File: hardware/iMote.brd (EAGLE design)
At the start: 43 x 50 mm, 50 parts, among them CN1 USB-MINIB-UX60SC-MB, CN2 ICSP, CN3 CC-HEADER, IC1 ATmega328P-AU, IC2 BLE112-A-VISUAL, IC3 FT232RLSSOP, Q1 16MHz, T1 2SC1815

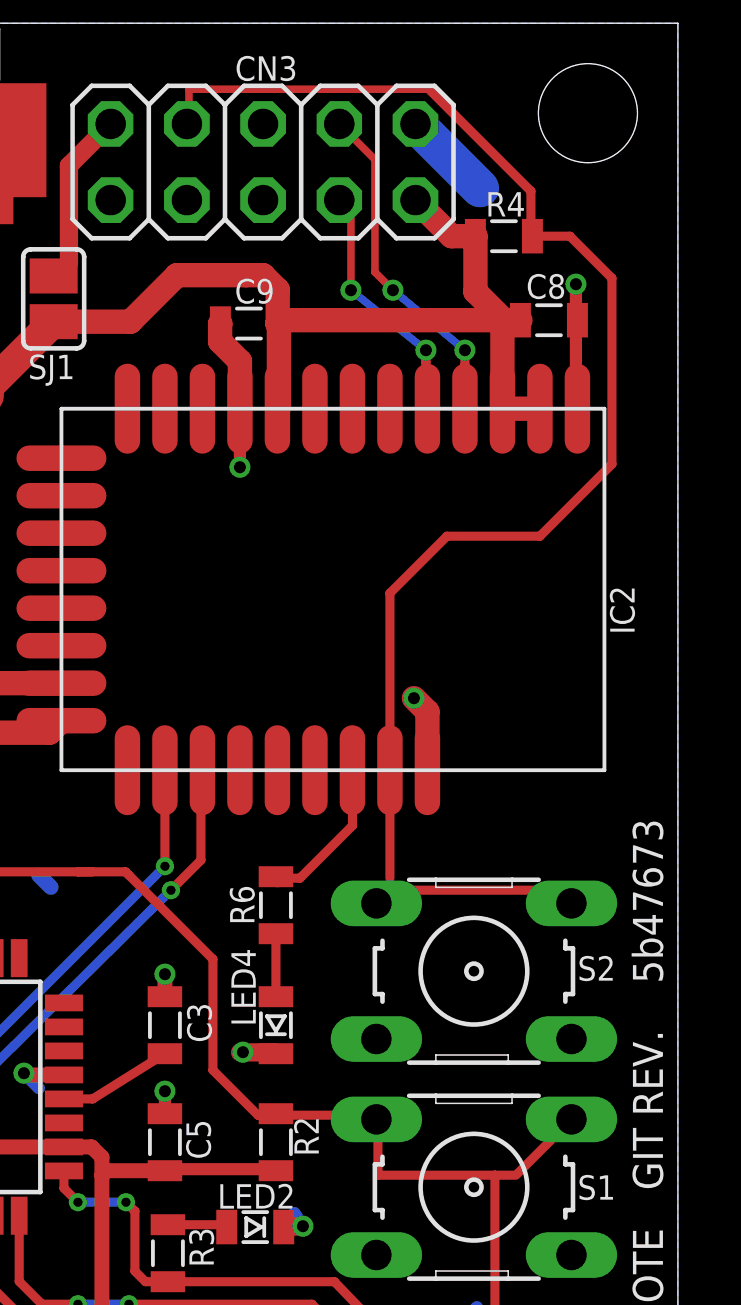
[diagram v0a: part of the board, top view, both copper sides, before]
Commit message: ble112をリセットするためのS2スイッチをなくして、 AVRの!RESET(5V)を分圧して3V程度にしてからble112の!BLE/RSTにつなぐ これはFT232RLのDTRからつながってるからUSB通したシリアル通信をしようとするときに AVRのリセットと同時にble112もリセットするから AVRの起動後からble112とのシリアル通信がうまくいく (この変更を行うまでは,シリアル通信開始時に必ずS2スイッチを押す必要があった)
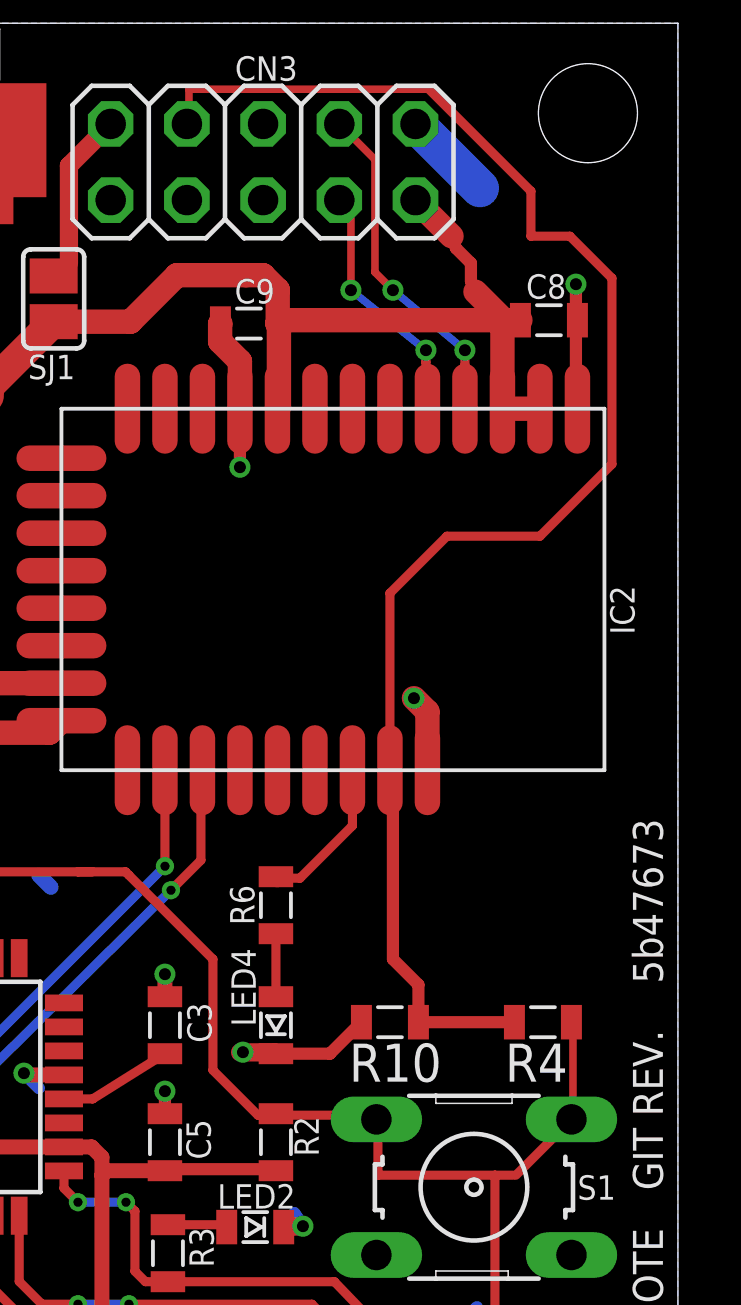
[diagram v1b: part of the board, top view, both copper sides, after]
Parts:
- removed S2: B3F-1000, switch-omron:B3F-10XX
- added R10: 22k, my:2012
- R4: value 1K -> 10k
- moved R4 26.2 mm to (38.5, 16.7)
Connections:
- net !BLE/RST: now also R10.2, R4.2; no longer R4.1, S2.1, S2.2
- net !RESET: now also R4.1
- net +3V3: no longer R4.2
- net GND: now also R10.1; no longer S2.3, S2.4
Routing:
- net !RESET: track 43.4 -> 46.8 mm
- net GND: track 90.2 -> 93.5 mm
- net +3V3: track 60.6 -> 60.1 mm
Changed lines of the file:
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@@
 <attribute name="VALUE" x="29.462" y="42.274" size="1.27" layer="27" rot="R180"/>
-</element>
-<element name="R4" library="my" package="2012" value="1K" x="37.2" y="42.9" smashed="yes" rot="R180">
-<attribute name="NAME" x="36.586" y="43.556" size="0.8128" layer="25"/>
-<attribute name="VALUE" x="37.962" y="45.186" size="1.27" layer="27" rot="R180"/>
-</element>
-<element name="S2" library="switch-omron" package="B3F-10XX" value="B3F-1000" x="36.2" y="18.4" smashed="yes">
-<attribute name="OC_NEWARK" value="36M3542" x="16.2" y="28.4" size="1.778" layer="27" display="off"/>
-<attribute name="MPN" value="B3F-1000" x="16.2" y="28.4" size="1.778" layer="27" display="off"/>
-<attribute name="MF" value="" x="16.2" y="28.4" size="1.778" layer="27" display="off"/>
-<attribute name="OC_FARNELL" value="176432" x="16.2" y="28.4" size="1.778" layer="27" display="off"/>
-<attribute name="NAME" x="39.652" y="18.083" size="0.8128" layer="25" ratio="10"/>
-<attribute name="VALUE" x="33.152" y="13.32" size="1.27" layer="27" ratio="10"/>
 </element>
 <element name="R5" library="my" package="2012" value="330" x="16" y="28" smashed="yes" rot="R270">
@@
 <attribute name="NAME" x="24.0038" y="0.0588" size="0.8128" layer="25" ratio="10"/>
 <attribute name="VALUE" x="22.58" y="-0.845" size="1.27" layer="27"/>
+</element>
+<element name="R4" library="my" package="2012" value="10k" x="38.5" y="16.7" smashed="yes" rot="R180">
+<attribute name="NAME" x="37.238" y="14.716" size="1.27" layer="25"/>
+<attribute name="VALUE" x="39.262" y="18.986" size="1.27" layer="27" rot="R180"/>
+</element>
+<element name="R10" library="my" package="2012" value="22k" x="33.4" y="16.7" smashed="yes">
+<attribute name="NAME" x="32.038" y="14.716" size="1.27" layer="25"/>
+<attribute name="VALUE" x="32.638" y="14.414" size="1.27" layer="27"/>
 </element>
 </elements>
@@
 <contactref element="C13" pad="2"/>
 <contactref element="S1" pad="1"/>
-<contactref element="S1" pad="2"/>
 <wire x1="39.4" y1="13.4" x2="37.6" y2="11.6" width="0.3048" layer="1"/>
 <wire x1="35.6" y1="2.4" x2="35.54" y2="2.33" width="0.254" layer="1"/>
-<wire x1="39.4" y1="13.4" x2="39.4512" y2="13.4606" width="0.254" layer="1"/>
 <wire x1="33" y1="11.6" x2="36.9" y2="11.6" width="0.3048" layer="1"/>
 <wire x1="36.9" y1="11.6" x2="37.5" y2="11.6" width="0.3048" layer="1"/>
@@
 <wire x1="35.6" y1="2.4" x2="36.9" y2="3.7" width="0.3048" layer="1"/>
 <wire x1="36.9" y1="3.7" x2="36.9" y2="11.6" width="0.3048" layer="1"/>
+<contactref element="S1" pad="2"/>
+<contactref element="R4" pad="1"/>
+<wire x1="39.5" y1="13.5" x2="39.4512" y2="13.4606" width="0.254" layer="1"/>
+<wire x1="39.5" y1="13.5" x2="39.4" y2="13.4" width="0.254" layer="1"/>
+<wire x1="39.5" y1="13.6" x2="39.5" y2="16.7" width="0.254" layer="1"/>
+<wire x1="39.5" y1="16.7" x2="39.45" y2="16.7" width="0.254" layer="1"/>
+<wire x1="39.5" y1="13.6" x2="39.4512" y2="13.4606" width="0.254" layer="1"/>
 </signal>
 <signal name="D11/MOSI">
@@
 <contactref element="C10" pad="2"/>
 <contactref element="C9" pad="2"/>
-<contactref element="S2" pad="3"/>
 <contactref element="LED3" pad="C"/>
 <contactref element="LED4" pad="C"/>
@@
 <contactref element="IC3" pad="18"/>
 <contactref element="S1" pad="4"/>
-<contactref element="S2" pad="4"/>
 <contactref element="IC1" pad="21"/>
 <contactref element="C5" pad="1"/>
@@
 <wire x1="22.05" y1="26.35" x2="19" y2="26.35" width="0.8128" layer="1"/>
 <wire x1="30.5" y1="9.9" x2="30.21575" y2="10.33793125" width="0.4064" layer="16"/>
+<contactref element="R10" pad="1"/>
+<wire x1="29.6" y1="15.65" x2="31.4" y2="15.65" width="0.4064" layer="1"/>
+<wire x1="31.4" y1="15.65" x2="32.45" y2="16.7" width="0.4064" layer="1"/>
 </signal>
 <signal name="N$10">
@@
 <contactref element="IC2" pad="DVDD"/>
 <contactref element="C10" pad="1"/>
-<contactref element="R4" pad="2"/>
 <contactref element="R5" pad="1"/>
 <contactref element="CN3" pad="2"/>
@@
 <wire x1="29.8" y1="40.1" x2="37.2" y2="40.1" width="0.8128" layer="1"/>
 <wire x1="37.2" y1="40.1" x2="37.75" y2="40.1" width="0.8128" layer="1"/>
-<wire x1="36.25" y1="42.9" x2="36.25" y2="41.05" width="0.8128" layer="1"/>
 <wire x1="36.25" y1="41.05" x2="37.2" y2="40.1" width="0.8128" layer="1"/>
-<wire x1="36.25" y1="42.9" x2="35.454" y2="42.9" width="0.8128" layer="1"/>
 <wire x1="35.454" y1="42.9" x2="34.252" y2="44.102" width="0.8128" layer="1"/>
 <wire x1="37.15" y1="37.15" x2="38.4" y2="37.15" width="0.8128" layer="1"/>
@@
 <wire x1="19" y1="28.25" x2="18.3" y2="28.95" width="0.8128" layer="1"/>
 <wire x1="18.3" y1="28.95" x2="16" y2="28.95" width="0.8128" layer="1"/>
+<wire x1="36.1" y1="42" x2="35.6" y2="42.5" width="0.4064" layer="1"/>
+<wire x1="36.1" y1="41.4" x2="36.1" y2="42" width="0.4064" layer="1"/>
+<wire x1="35.6" y1="42.5" x2="35.454" y2="42.9" width="0.4064" layer="1"/>
+<wire x1="36.1" y1="41.4" x2="36.25" y2="41.05" width="0.4064" layer="1"/>
 </signal>
 <signal name="!BLE/RST">
-<contactref element="R4" pad="1"/>
-<contactref element="S2" pad="1"/>
 <contactref element="IC2" pad="RESET"/>
 <contactref element="CN3" pad="7"/>
-<contactref element="S2" pad="2"/>
 <wire x1="26.7" y1="47.8" x2="34.7" y2="47.8" width="0.254" layer="1"/>
 <wire x1="26.7" y1="46.7" x2="26.7" y2="47.8" width="0.254" layer="1"/>
-<wire x1="38.1" y1="42.9" x2="38.15" y2="42.9" width="0.254" layer="1"/>
 <wire x1="26.7" y1="46.7" x2="26.632" y2="46.642" width="0.254" layer="1"/>
-<wire x1="33.4" y1="21.5" x2="33.4" y2="25.1" width="0.3048" layer="1"/>
 <wire x1="33.4" y1="25.2" x2="33.4" y2="25.1" width="0.254" layer="1"/>
 <wire x1="33.4" y1="25.2" x2="33.4" y2="31" width="0.3048" layer="1"/>
@@
 <wire x1="35.3" y1="32.9" x2="38.4" y2="32.9" width="0.3048" layer="1"/>
 <wire x1="38.4" y1="32.9" x2="40.8" y2="35.3" width="0.3048" layer="1"/>
-<wire x1="33.4" y1="21.1" x2="33" y2="20.7" width="0.3048" layer="1"/>
-<wire x1="33.4" y1="21.4" x2="33.4" y2="21.1" width="0.254" layer="1"/>
-<wire x1="33" y1="20.7" x2="32.9488" y2="20.6606" width="0.254" layer="1"/>
-<wire x1="33.4" y1="21.4" x2="33.4" y2="21.5" width="0.254" layer="1"/>
-<wire x1="39.4" y1="21.1" x2="33.5" y2="21.1" width="0.3048" layer="1"/>
-<wire x1="39.4" y1="20.7" x2="39.4" y2="21.1" width="0.3048" layer="1"/>
-<wire x1="33.5" y1="21.1" x2="32.9488" y2="20.6606" width="0.3048" layer="1"/>
-<wire x1="39.4" y1="20.7" x2="39.4512" y2="20.6606" width="0.3048" layer="1"/>
 <wire x1="38.1" y1="42.9" x2="39.4" y2="42.9" width="0.3048" layer="1"/>
 <wire x1="39.4" y1="42.9" x2="40.8" y2="41.5" width="0.3048" layer="1"/>
@@
 <wire x1="38.1" y1="42.9" x2="38.1" y2="44.4" width="0.3048" layer="1"/>
 <wire x1="38.1" y1="44.4" x2="34.7" y2="47.8" width="0.3048" layer="1"/>
+<contactref element="R4" pad="2"/>
+<contactref element="R10" pad="2"/>
+<wire x1="37.5" y1="16.7" x2="34.4" y2="16.7" width="0.4064" layer="1"/>
+<wire x1="34.4" y1="16.7" x2="34.35" y2="16.7" width="0.254" layer="1"/>
+<wire x1="37.5" y1="16.7" x2="37.55" y2="16.7" width="0.254" layer="1"/>
+<wire x1="33.4" y1="25.1" x2="33.5" y2="25.1" width="0.4064" layer="1"/>
+<wire x1="33.5" y1="25.1" x2="33.5" y2="18.8" width="0.4064" layer="1"/>
+<wire x1="33.5" y1="18.8" x2="34.35" y2="17.95" width="0.4064" layer="1"/>
+<wire x1="34.35" y1="17.95" x2="34.35" y2="16.7" width="0.4064" layer="1"/>
 </signal>
 <signal name="N$5">

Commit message: 回路修正しました
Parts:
- removed LED5: USB/TX, my:LED-2012
- removed LED6: USB/RX, my:LED-2012
- removed R7, R8: 680, my:2012
- removed RB: 4.7k, my:2012
- added Q2: BSS138, m-pad-2.1:SOT23
- added R11: 2.2k, my:2012
- added R12: 3.3k, my:2012
- added R13, RB1: 4.7k, my:2012
- added R14, RB2: 10k, my:2012
- added R15: 820, my:2012
- added R16: 750, my:2012
- added R17: 1K, my:2012
- CN4: value (none) -> IRLED_Conn
- CN5: value (none) -> PIN_Header
- LED2: value ICSP -> 5V
- LED3: value 3.3V -> 5V
- LED4: value BLE -> OSTB0603C1C-A; device my:LED-2012 -> FullColorLED:OSTB0603C1C
- R10: value 22k -> 3.3k
- R4: value 10k -> 2.2k
- R5: value 330 -> 1K
- T1: value 2SC1815 -> 2SD1718; device transistor:TO92-ECB -> transistor:SC59-BEC
- moved LED2 42.9 mm to (7.80, 47.2), turned to 90 degrees
- moved R3 39.5 mm to (7.80, 44.1), turned to 90 degrees
- moved R6 31.0 mm to (9.40, 44.1)
- moved LED3 23.4 mm to (9.40, 47.2), turned to 90 degrees
- moved R5 21.7 mm to (15.7, 6.30), turned to 180 degrees
- moved LED4 19.7 mm to (12.3, 7.25), turned to 90 degrees
- moved R4 8.85 mm to (31.2, 21.7), turned to 270 degrees
- moved C13 5.65 mm to (16.1, 27.3), turned to 270 degrees
- moved R10 5.00 mm to (33.4, 21.7), turned to 90 degrees
- moved C3 3.00 mm to (27.4, 14.0)
- moved S1 2.47 mm to (37.5, 13.3), turned to 90 degrees
- moved C5 2.42 mm to (27.4, 10.8), turned to 90 degrees
- moved RC 1.91 mm to (6.60, 22.5), turned to 180 degrees
- moved C4 1.33 mm to (11.8, 15.5)
- moved LED1 1.17 mm to (3.70, 41.6)
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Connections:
- removed net D5/BLETX: IC1.9, IC2.P0_5
- removed net D6/BLERX: IC1.10, IC2.P0_4
- removed net D7: CN5.1, IC1.11
- removed net N$13: LED4.A, R6.1
- removed net N$7: LED2.A, R3.1
- new net A0/BTN: IC1.23, R2.1, S1.1, S1.2
- new net A1/RST_HV: IC1.24, R4.2
- new net A3/TX_HV: IC1.26, R11.2
- new net A4/RX_HV: IC1.27, Q2.3, R14.1
- new net D5/LED_B: IC1.9, R16.1
- new net D6/LED_G: IC1.10, R15.1
- new net D7/LED_R: IC1.11, R5.1
- new net N$15: LED4.GREEN, R15.2
- new net N$17: LED4.BLUE, R16.2
- new net RX_LV/BLERX: IC2.P0_4, R11.1, R12.2
- new net TX_LV/BLETX: IC2.P0_5, Q2.2, R13.1
- net !BLE/RST: now also R4.1; no longer R4.2
- net !RESET: now also R17.1; no longer R2.1, R4.1, S1.1, S1.2
- net +3V3: now also Q2.1, R13.2; no longer R5.1
- net +5V: now also LED4.ANODE, R14.2, R17.2
- net BLE/P0_0: no longer R6.2
- net D13/SCK: no longer R3.2
- net D3/IROUT: now also RB1.2; no longer RB.2
- net GND: now also R12.1; no longer LED4.C, LED5.C, LED6.C
- net N$10: now also RB1.1, RB2.1; no longer RB.1
- net N$11: now also RB2.2
- net N$4: now also LED2.A, R3.2; no longer LED5.A, R7.1
- net N$5: now also LED4.RED; no longer LED3.A
- net N$6: now also LED3.A, R6.2; no longer LED6.A, R8.1
- net USB/RXLED: now also R6.1; no longer R8.2
- net USB/TXLED: now also R3.1; no longer R7.2
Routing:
- net A0/BTN: track 0.00 -> 23.0 mm
- net D6/BLERX: track 19.4 -> 0.00 mm, vias 2 -> 0
- net D5/BLETX: track 19.2 -> 0.00 mm, vias 2 -> 0
- net +5V: track 87.4 -> 104.1 mm
- net A4/RX_HV: track 0.00 -> 12.7 mm, vias 0 -> 2
- net +3V3: track 60.1 -> 72.4 mm
- net D7: track 11.5 -> 0.00 mm, vias 2 -> 0
- net A1/RST_HV: track 0.00 -> 11.1 mm
- net GND: track 93.5 -> 104.5 mm
- net A3/TX_HV: track 0.00 -> 8.12 mm
- net !BLE/RST: track 52.1 -> 45.7 mm
- net TX_LV/BLETX: track 0.00 -> 6.06 mm
- net N$8: track 15.7 -> 10.2 mm
- net BLE/P0_0: track 5.20 -> 0.00 mm
- net RX_LV/BLERX: track 0.00 -> 4.90 mm
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
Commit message: 回路修正_暫定版です
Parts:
- removed CN5: PIN_Header, my:PINHEAD-1X03
- removed LED2, LED3: 5V, my:LED-2012
- removed Q1: 16MHz, my:XTAL-HC-49/S
- removed R10: 3.3k, my:2012
- removed R11: 2.2k, my:2012
- removed R16: 750, my:2012
- removed R17: 1K, my:2012
- added R7: 2.2k, my:2012
- added R8: 3.3k, my:2012
- added Y1: 16MHz, my:XTAL-HC-49/S
- C11: value 4.7uF -> 0.1uF
- C13: value 0.1uF -> 4.7uF
- CN3: value CC-HEADER -> PIN_Header; device pinhead:2X05 -> my:PINHEAD-1X03
- CN4: value IRLED_Conn -> CC-HEADER; device pinhead:1X02 -> pinhead:2X05
- LED4: value OSTB0603C1C-A -> 5MMRGBLED; device FullColorLED:OSTB0603C1C -> adafruit:LED5MMRGB
- R1: value 330 -> 10K
- R12: value 3.3k -> 1.2K
- R13: value 4.7k -> 2.4k
- R14: value 10k -> 1k
- R15: value 820 -> 200
- R3: value 330 -> 10k
- R4: value 2.2k -> 4.7k
- R5: value 1K -> 2.2k
- R6: value 330 -> 3.3k
- R9: value 200 -> 220
- S1: value B3F-1000 -> S1; device switch-omron:B3F-10XX -> switch-omron:B3F-31XX
- moved R1 40.4 mm to (33.4, 12.0), turned to 270 degrees
- moved C11 36.5 mm to (25.4, 38.0), turned to 90 degrees
- moved R9 35.9 mm to (10.0, 38.6), turned to 180 degrees
- moved CN4 35.8 mm to (35.5, 45.3), turned to 180 degrees
- moved C13 35.6 mm to (41.5, 2.35)
- moved R6 34.0 mm to (35.3, 22.0)
- moved CN3 32.5 mm to (46.9, 17.8), turned to 90 degrees
- moved S1 32.3 mm to (7.42, 25.0), turned to 270 degrees
- moved D1 29.1 mm to (25.0, 2.49), turned to 180 degrees
- moved PL-IRM1 26.0 mm to (37.0, 2.20)
- moved R3 25.9 mm to (15.8, 19.4), turned to 180 degrees
- moved R15 25.9 mm to (41.4, 5.48), turned to 90 degrees
- moved RC 24.8 mm to (19.7, 1.40), turned to 0 degrees
- moved T1 23.7 mm to (20.2, 4.00), turned to 90 degrees
- moved R5 23.5 mm to (33.2, 22.0), turned to 270 degrees
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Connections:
- removed net A0/BTN: IC1.23, R2.1, S1.1, S1.2
- removed net A1/RST_HV: IC1.24, R4.2
- removed net D10: CN5.3, IC1.14
- removed net D5/LED_B: IC1.9, R16.1
- removed net D7/LED_R: IC1.11, R5.1
- removed net D9: CN5.2, IC1.13
- removed net N$4: LED2.A, R3.2
- removed net N$6: LED3.A, R6.2
- removed net USB/RXLED: IC3.22, R6.1
- removed net USB/TXLED: IC3.23, R3.1
- new net A0: CN3.2, IC1.23
- new net A1: CN3.3, IC1.24
- new net A2/BTN: R2.1, S1.2
- new net A2/RST_HV: IC1.25, R7.2
- new net A7: CN3.1, IC1.22
- new net D10/IRIN: IC1.14, PL-IRM1.1
- new net D2_BTN: IC1.32
- new net D5/LED_R: IC1.9, R12.1
- new net D7/LED_B: IC1.11, R14.1
- new net D9/IROUT: IC1.13, RB1.2
- net !BLE/RST: now also CN4.7, R7.1, R8.2; no longer CN3.7, R10.2, R4.1
- net !RESET: now also C12.2, R1.1; no longer C13.2, R17.1
- net +3V3: now also C11.1, CN4.2, R4.2; no longer C12.1, CN3.2, R13.2
- net +5V: now also C3.2, R1.2, R15.2, R3.2, R9.1; no longer C5.2, CN4.1, LED4.ANODE, R1.1, R14.2, R17.2, R9.2
- net A3/TX_HV: now also R5.2; no longer R11.2
- net A4/RX_HV: now also R3.1; no longer R14.1
- net AREF: now also C5.2; no longer C3.2
- net BLE/P2_1: now also CN4.4; no longer CN3.4
- net BLE/P2_2: now also CN4.3; no longer CN3.3
- net D3/IROUT: no longer RB1.2
- net D6/LED_G: now also R13.1; no longer R15.1
- net D8/IRIN: no longer PL-IRM1.1
- net GND: now also C13.2, CN4.1, LED4.3, R6.1, R8.1, S1.1; no longer C12.2, CN3.1, LED2.C, LED3.C, R10.1, R12.1, S1.3, S1.4
- net IRLED: no longer CN4.2
- net N$1: now also Y1.1; no longer Q1.1
- net N$15: now also LED4.2, R13.2; no longer LED4.GREEN, R15.2
- net N$16: now also C13.1, R15.1; no longer C11.1, R9.1
- net N$17: now also LED4.1, R14.2; no longer LED4.BLUE, R16.2
- net N$2: now also Y1.2; no longer Q1.2
- net N$3: now also R9.2; no longer R1.2
- net N$5: now also LED4.4, R12.2; no longer LED4.RED, R5.2
- net N$8: now also C12.1; no longer C13.1
- net PRG/VDD: now also CN4.9; no longer CN3.9
- net RX_LV/BLERX: now also R5.1, R6.2; no longer R11.1, R12.2
- net TX_LV/BLETX: now also R4.1; no longer R13.1
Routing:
- net A0/BTN: track 23.0 -> 0.00 mm
- net A1: track 0.00 -> 21.2 mm
- net A0: track 0.00 -> 20.4 mm
- net A7: track 0.00 -> 20.4 mm
- net D10/IRIN: track 0.00 -> 15.9 mm, vias 0 -> 2
- net D8/IRIN: track 15.3 -> 0.00 mm
- net D10: track 13.8 -> 0.00 mm
- net A2/RST_HV: track 0.00 -> 13.3 mm
- net A2/BTN: track 0.00 -> 13.0 mm
- net D9: track 12.3 -> 0.00 mm
- net A1/RST_HV: track 11.1 -> 0.00 mm
- net USB/TXLED: track 8.63 -> 0.00 mm, vias 2 -> 0
- net D5/LED_R: track 0.00 -> 8.50 mm
- net USB/RXLED: track 8.44 -> 0.00 mm, vias 2 -> 0
- net D11/MOSI: track 16.0 -> 24.4 mm, vias 3 -> 1
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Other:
- board size 43 x 50 mm -> 50 x 50 mm
